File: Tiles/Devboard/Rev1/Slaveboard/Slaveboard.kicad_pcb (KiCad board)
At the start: 4 copper layers, 90.5 x 87.8 mm, 41 parts, among them J1 Conn_01x05_Pin, SW1 TS-1178A, U1 CH32V003FxPx

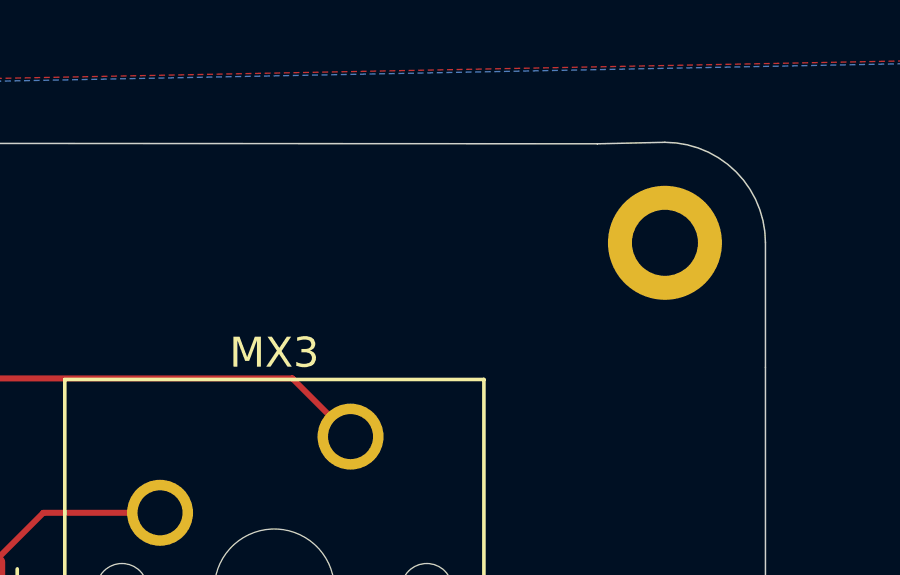
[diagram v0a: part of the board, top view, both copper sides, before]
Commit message: Added Silkscreen QoL
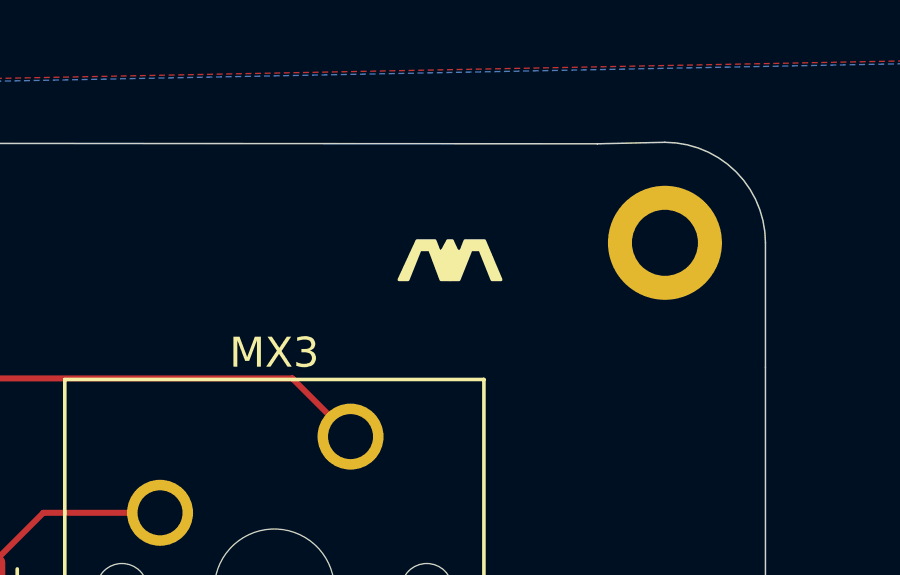
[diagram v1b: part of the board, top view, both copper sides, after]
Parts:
- renumbered SW1 to RESET
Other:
- board text added: "3V3"
- board text added: "GND"
- board text added: "Magnetile 4x4 Matrix Rev1"
- board text added: "SCL"
- board text added: "SDA"
- board text added: "SWIO"
